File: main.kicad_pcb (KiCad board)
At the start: 4 copper layers, 62.5 x 46.2 mm, 35 parts, among them J1 inductor connector, J2 inductor connector, J3 test point, J4 test point, J5 PWR, J6 pulse width selector, Q1 T60NO2R, U1 NE555P, U2 NE555P

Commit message: more details
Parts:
- added F1: 2A, Resistor_SMD:R_2512_6332Metric, B.Cu at (133.1, 90.4)
- C14: value 1nF -> 10nF
- D1: value 1N4148 -> SS34
- J5: value PWR -> IN; moved to B.Cu
- moved D2 4.07 mm to (130.6, 96.0)
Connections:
- D2 pad 2: VCC -> Net-(D2-Pad2)
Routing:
- net Net-(D2-Pad2): track 0.00 -> 3.36 mm
- net VCC: track 5.15 -> 5.97 mm

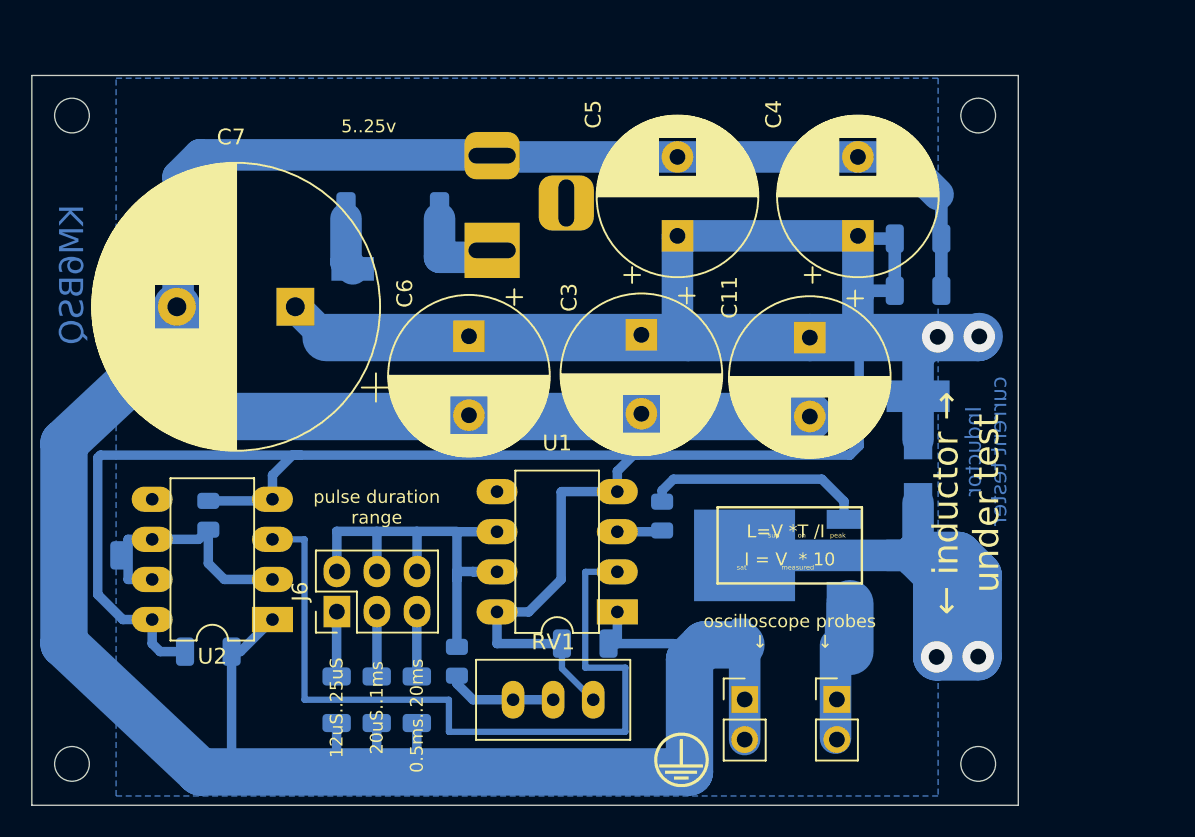
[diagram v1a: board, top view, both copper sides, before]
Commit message: Changed gate resistor Add heat map
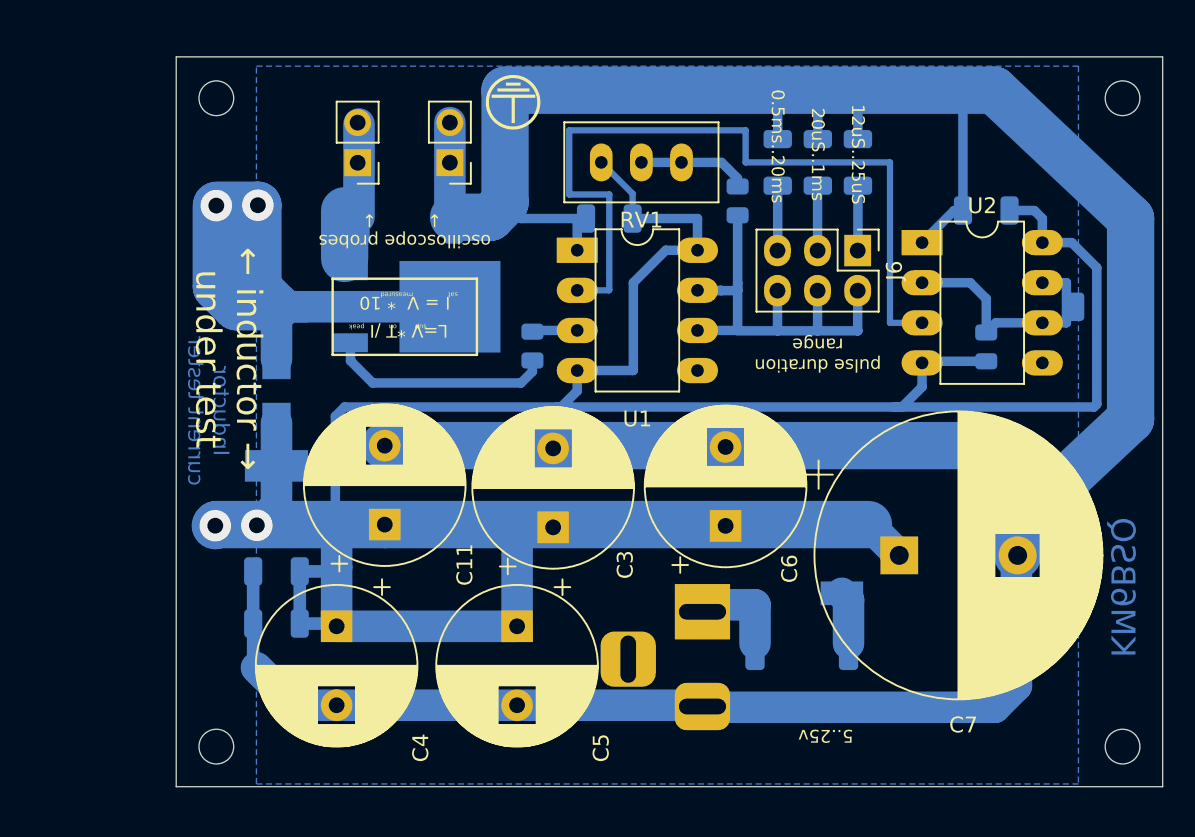
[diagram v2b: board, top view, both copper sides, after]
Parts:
- moved H2 78.8 mm to (179.3, 82.8), turned to 180 degrees
- moved H4 77.6 mm to (179.3, 123.9), turned to 180 degrees
- moved C14 65.4 mm to (177.8, 96.0), turned to 0 degrees
- moved H1 64.1 mm to (121.9, 82.8), turned to 180 degrees
- moved H3 62.7 mm to (121.9, 123.9), turned to 180 degrees
- moved C12 56.6 mm to (170.7, 89.9), turned to 180 degrees
- moved R1 50.4 mm to (170.7, 98.6), turned to -90 degrees
- moved U2 47.6 mm to (166.6, 91.9), turned to 0 degrees
- moved C8 47.4 mm to (162.6, 86.9), turned to 90 degrees
- moved C10 47.4 mm to (125.7, 116.1), turned to 180 degrees
- moved J3 45.6 mm to (130.9, 86.9), turned to 180 degrees
- moved C9 44.4 mm to (125.7, 112.8), turned to 180 degrees
- moved C2 44.0 mm to (160.0, 86.9), turned to 90 degrees
- moved J2 43.6 mm to (125.7, 96.0), turned to 90 degrees
- moved G*** 43.0 mm to (140.7, 83.1), turned to 180 degrees
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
